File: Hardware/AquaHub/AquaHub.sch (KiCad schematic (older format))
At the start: 73 parts, among them J10 PinHeader6, J13 PinHeader2, J14 PinHeader3, Q2 2SC1815, SW1 SW_Push, SW2 SW_Push, SW3 SW_Push, SW4 SW_Push, SW5 SW_Push, SW6 SW_Push, U1 ESP32-WROOM, U3 1A 3.3V, U4 Low-Side Driver, U5 1A 5V, U6 TCA9534, U7 DS1307+, U8 TPIC2810D, Y1 32.768KHz

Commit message: Commit latest hardware updates and initial firmware
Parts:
- BT1: footprint AquaFootprints:Multicomp-BC-2001 -> Battery:BatteryHolder_Multicomp_BC-2001_1x2032; Mouser (none) -> 534-1058; manf# (none) -> x
- C3: Mouser (none) -> TAJB106K006SNJ; manf# TAJB106K006SNJ -> (none)
- C4: Farnell (none) -> CA06848; Mouser (none) -> TAJD107K006SNJ; manf# TAJD107K006SNJ -> (none)
- C5, C6: Farnell (none) -> CA07886; Mouser (none) -> UWX1H100MCL1GB; manf# UWX1H100MCL1GB -> x
- C7, C8: Mouser (none) -> UWX1H4R7MCL1GB; manf# UWX1H4R7MCL1GB -> x
- C9: Farnell (none) -> CA07658
- LS1: Mouser (none) -> PS1240P02BT; manf# PS1240P02BT -> (none)
- Q2: Farnell (none) -> SC06581
- R10, R11, R12, R13, R14, R15, R16: Farnell (none) -> RE07105; Mouser (none) -> GWCR0603-4K7FT5; manf# GWCR0603-4K7FT5 -> (none)
- R3, R7: Mouser (none) -> GWCR0603-10KFT5; manf# GWCR0603-10KFT5 -> (none)
- R4, R5, R6: manf# GWCR0603-4K7FT5 -> (none)
- R8, R9: Farnell (none) -> RE07090; Mouser (none) -> GWCR0603-4K7FT5; manf# GWCR0603-4K7FT5 -> (none)
- U1: Mouser (none) -> ESP32-WROOM-32D; manf# ESP32-WROOM-32D -> x
- U3: Mouser (none) -> NCP1117DT33G; manf# NCP1117DT33G -> x
- U4: Mouser (none) -> TPL7407LADR; manf# TPL7407LADR -> x
- U5: Mouser (none) -> NCP1117DT50G; manf# NCP1117DT50G -> x
- U6: Mouser (none) -> TCA9534DWR; manf# TCA9534DWR -> x
- U7: manf# (none) -> x
- U8: RS (none) -> 660-7981
- Y1: Mouser (none) -> 815-AB26T-32.768KHZ; manf# (none) -> z

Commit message: Added some more framework
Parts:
- added SW?: Reset, Button_Switch_THT:SW_CK_D6R_SPST_12mm_H14.3mm, symbol AquaHub-rescue:SW_CK_D6R_SPST-Switch
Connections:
- net EN: no longer R3.2, U1.3 (EN)
- net GND: now also SW?.2 (B), SW?.4 (B)
- new net: R3.2, SW?.1 (A), SW?.3 (A), U1.3 (EN)
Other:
- moved on the sheet: C3, C4, R3
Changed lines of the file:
@@
 L AquaHub-rescue:C_Small-Device C3
 U 1 1 5BB06BF9
-P 5525 3250
-F 0 "C3" H 5400 3325 50  0000 L CNN
-F 1 "10uF" H 5325 3175 50  0000 L CNN
-F 2 "Capacitor_SMD:C_0805_2012Metric_Pad1.15x1.40mm_HandSolder" H 5563 3100 50  0001 C CNN
-F 3 "~" H 5525 3250 50  0001 C CNN
-F 4 "Mouser" H 3975 2100 50  0001 C CNN "Vendor"
-F 5 "TAJB106K006SNJ" H 0   0   50  0001 C CNN "Mouser"
-	1    5525 3250
+P 5250 3250
+F 0 "C3" H 5125 3325 50  0000 L CNN
+F 1 "10uF" H 5050 3175 50  0000 L CNN
+F 2 "Capacitor_SMD:C_0805_2012Metric_Pad1.15x1.40mm_HandSolder" H 5288 3100 50  0001 C CNN
+F 3 "~" H 5250 3250 50  0001 C CNN
+F 4 "Mouser" H 3700 2100 50  0001 C CNN "Vendor"
+F 5 "TAJB106K006SNJ" H -275 0   50  0001 C CNN "Mouser"
+	1    5250 3250
 	1    0    0    -1
 $EndComp
@@
 L AquaHub-rescue:CP_Small-Device C4
 U 1 1 5BB06BFF
-P 5725 3250
-F 0 "C4" H 5750 3325 50  0000 L CNN
-F 1 "100uF" H 5750 3175 50  0000 L CNN
-F 2 "Capacitor_Tantalum_SMD:CP_EIA-7343-31_Kemet-D_Pad2.25x2.55mm_HandSolder" H 5763 3100 50  0001 C CNN
-F 3 "~" H 5725 3250 50  0001 C CNN
-F 4 "Mouser" H 3975 2100 50  0001 C CNN "Vendor"
-F 5 "CA06848" H 0   0   50  0001 C CNN "Farnell"
-F 6 "TAJD107K006SNJ" H 0   0   50  0001 C CNN "Mouser"
-	1    5725 3250
-	1    0    0    -1
-$EndComp
-Wire Wire Line
-	5525 3350 5525 3400
-Wire Wire Line
-	5525 3400 5625 3400
-Wire Wire Line
-	5725 3400 5725 3350
-Wire Wire Line
-	5625 3400 5625 3450
-Connection ~ 5625 3400
-Wire Wire Line
-	5625 3400 5725 3400
-Wire Wire Line
-	5525 3150 5525 3100
-Wire Wire Line
-	5525 3100 5625 3100
-Wire Wire Line
-	5725 3100 5725 3150
-Wire Wire Line
-	5625 3100 5625 3050
-Connection ~ 5625 3100
-Wire Wire Line
-	5625 3100 5725 3100
+P 5450 3250
+F 0 "C4" H 5475 3325 50  0000 L CNN
+F 1 "100uF" H 5475 3175 50  0000 L CNN
+F 2 "Capacitor_Tantalum_SMD:CP_EIA-7343-31_Kemet-D_Pad2.25x2.55mm_HandSolder" H 5488 3100 50  0001 C CNN
+F 3 "~" H 5450 3250 50  0001 C CNN
+F 4 "Mouser" H 3700 2100 50  0001 C CNN "Vendor"
+F 5 "CA06848" H -275 0   50  0001 C CNN "Farnell"
+F 6 "TAJD107K006SNJ" H -275 0   50  0001 C CNN "Mouser"
+	1    5450 3250
+	1    0    0    -1
+$EndComp
+Wire Wire Line
+	5250 3350 5250 3400
+Wire Wire Line
+	5250 3400 5350 3400
+Wire Wire Line
+	5450 3400 5450 3350
+Connection ~ 5350 3400
+Wire Wire Line
+	5350 3400 5450 3400
+Wire Wire Line
+	5250 3150 5250 3100
+Wire Wire Line
+	5250 3100 5350 3100
+Wire Wire Line
+	5450 3100 5450 3150
+Wire Wire Line
+	5350 3100 5350 3050
+Connection ~ 5350 3100
+Wire Wire Line
+	5350 3100 5450 3100
 $Comp
 L AquaHub-rescue:GND-power #PWR0106
 U 1 1 5BB06C11
-P 5625 3450
-F 0 "#PWR0106" H 5625 3200 50  0001 C CNN
-F 1 "GND" H 5630 3277 50  0000 C CNN
-F 2 "" H 5625 3450 50  0001 C CNN
-F 3 "" H 5625 3450 50  0001 C CNN
-	1    5625 3450
-	1    0    0    -1
-$EndComp
-Wire Wire Line
-	5625 3050 6150 3050
+P 5350 3500
+F 0 "#PWR0106" H 5350 3250 50  0001 C CNN
+F 1 "GND" H 5355 3327 50  0000 C CNN
+F 2 "" H 5350 3500 50  0001 C CNN
+F 3 "" H 5350 3500 50  0001 C CNN
+	1    5350 3500
+	1    0    0    -1
+$EndComp
 $Comp
 L AquaHub-rescue:Conn_01x02-Connector_Generic J13
@@
 L AquaHub-rescue:R-Device R3
 U 1 1 5BA87CFB
-P 6150 3300
-F 0 "R3" H 6200 3375 50  0000 L CNN
-F 1 "10k" H 6200 3300 50  0000 L CNN
-F 2 "Resistor_SMD:R_0603_1608Metric_Pad1.05x0.95mm_HandSolder" V 6080 3300 50  0001 C CNN
-F 3 "~" H 6150 3300 50  0001 C CNN
-F 4 "Mouser" H 3975 2100 50  0001 C CNN "Vendor"
-F 5 "GWCR0603-10KFT5" H 0   0   50  0001 C CNN "Mouser"
-	1    6150 3300
-	1    0    0    -1
-$EndComp
-Text Label 6150 3500 1    39   ~ 0
-EN
+P 6150 3275
+F 0 "R3" H 6200 3350 50  0000 L CNN
+F 1 "10k" H 6200 3275 50  0000 L CNN
+F 2 "Resistor_SMD:R_0603_1608Metric_Pad1.05x0.95mm_HandSolder" V 6080 3275 50  0001 C CNN
+F 3 "~" H 6150 3275 50  0001 C CNN
+F 4 "Mouser" H 3975 2075 50  0001 C CNN "Vendor"
+F 5 "GWCR0603-10KFT5" H 0   -25 50  0001 C CNN "Mouser"
+	1    6150 3275
+	1    0    0    -1
+$EndComp
 $Comp
 L AquaHub-rescue:R-Device R7
@@
 	7425 4700 7150 4700
 Wire Wire Line
-	6150 3150 6150 3050
+	6150 3125 6150 3050
 Wire Wire Line
 	6150 3050 6350 3050
@@
 	6350 3050 6350 2900
 Wire Wire Line
-	6150 3450 6150 3500
-Connection ~ 6150 3050
+	6150 3425 6150 3450
 Wire Wire Line
 	4875 5300 4900 5300
@@
 NoConn ~ 5350 4000
 NoConn ~ 5350 3900
+$Comp
+L AquaHub-rescue:SW_CK_D6R_SPST-Switch SW?
+U 1 1 5BD9B1CF
+P 5800 3450
+AR Path="/5B8F2634/5BD9B1CF" Ref="SW?"  Part="1"
+AR Path="/5BD9B1CF" Ref="SW?"  Part="1"
+F 0 "SW?" H 5800 3550 50  0000 C CNN
+F 1 "Reset" H 5700 3600 50  0000 L CNN
+F 2 "Button_Switch_THT:SW_CK_D6R_SPST_12mm_H14.3mm" H 5800 3650 50  0001 C CNN
+F 3 "" H 5800 3650 50  0001 C CNN
+F 4 "Mouser" H -1175 -875 50  0001 C CNN "Vendor"
+	1    5800 3450
+	-1   0    0    1
+$EndComp
+Wire Wire Line
+	5350 3050 6150 3050
+Wire Wire Line
+	6150 3450 6000 3450
+Connection ~ 6150 3450
+Wire Wire Line
+	6150 3450 6150 3500
+Wire Wire Line
+	5350 3400 5350 3450
+Wire Wire Line
+	5600 3450 5350 3450
+Connection ~ 5350 3450
+Wire Wire Line
+	5350 3450 5350 3500
+Connection ~ 6150 3050
 $EndSCHEMATC

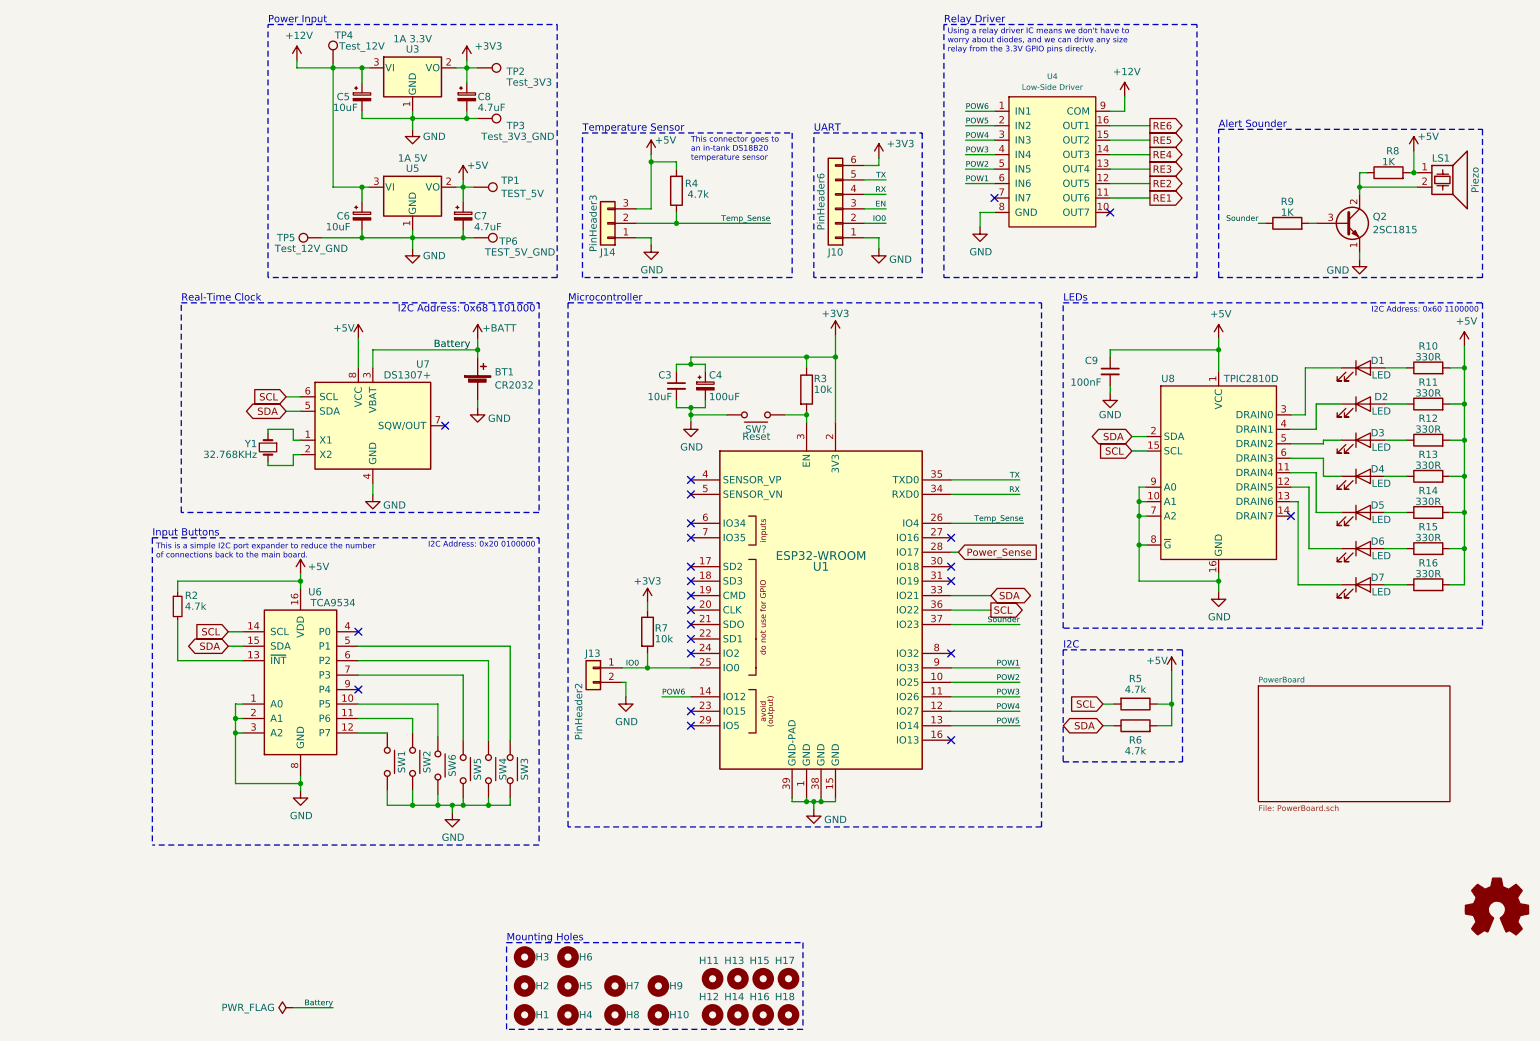
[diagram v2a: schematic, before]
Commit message: Big PCB switch to a single board. Again.
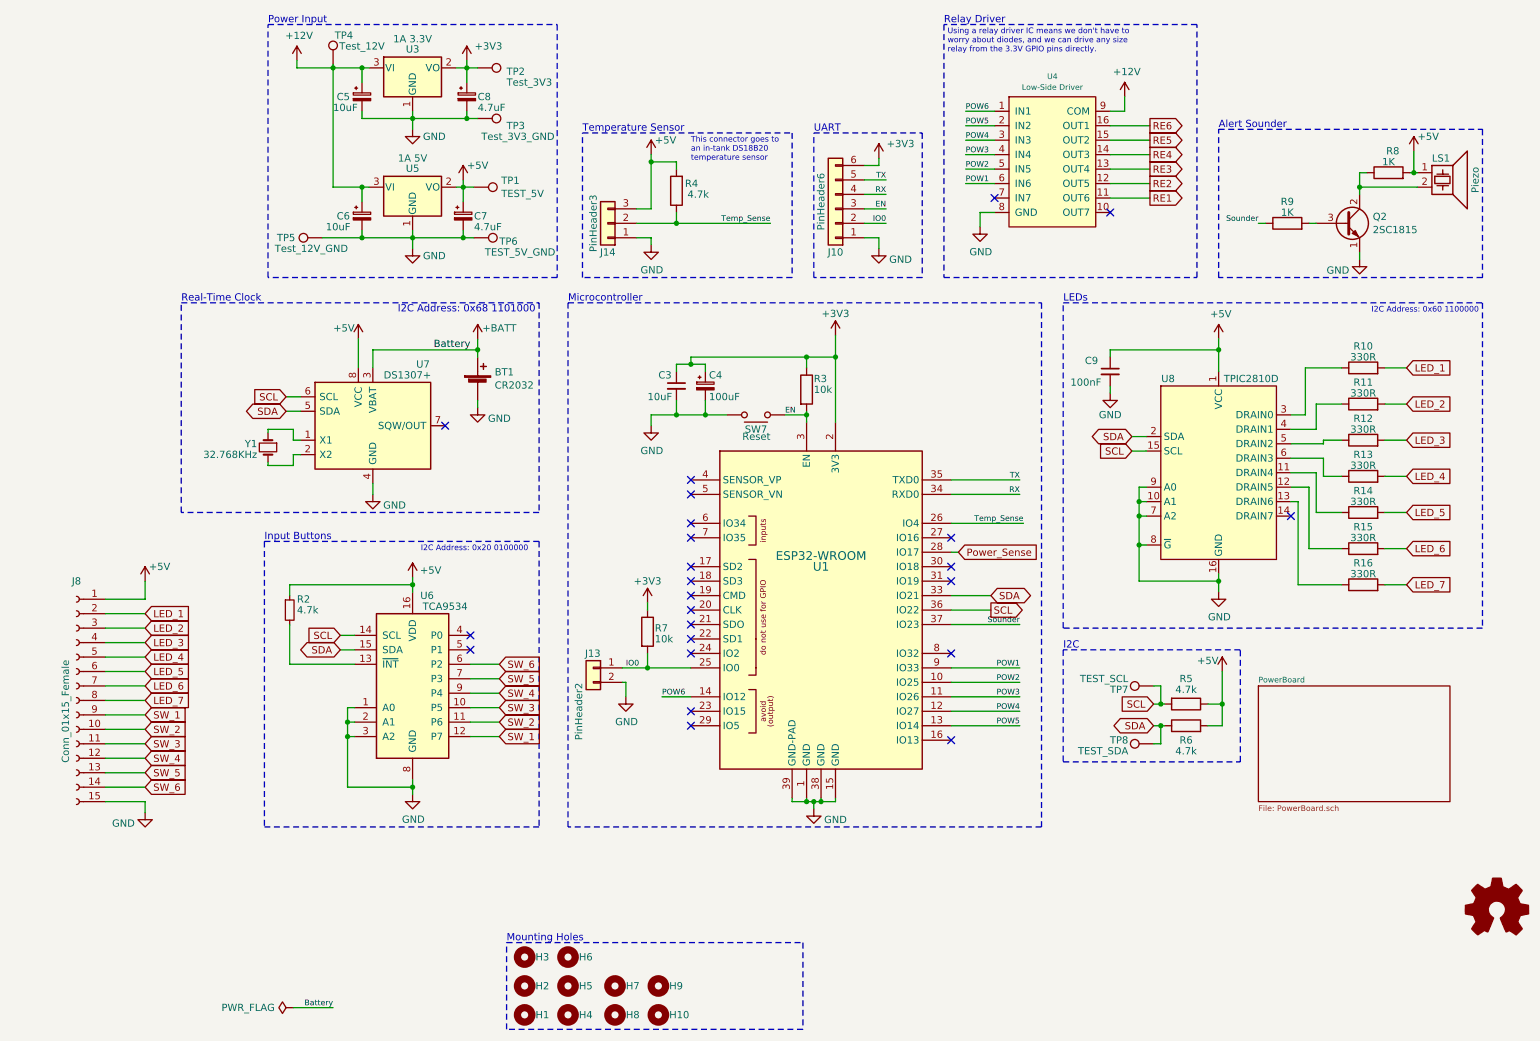
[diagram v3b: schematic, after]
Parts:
- removed D1, D2, D3, D4, D5, D6, D7: LED, LED_THT:LED_D5.0mm, symbol Device:LED
- removed H11, H12, H13, H14, H15, H16, H17, H18: MountingHole, AquaFootprints:Breakaway 1mm, symbol Mechanical:MountingHole
- removed SW1, SW2, SW3, SW4, SW5, SW6: SW_Push, Button_Switch_THT:SW_CK_D6R_SPST_12mm_H14.3mm, symbol AquaHub-rescue:SW_CK_D6R_SPST-Switch
- added J8: Conn_01x15_Female, Connector_Hirose:Hirose_DF52-15S-0.8H_1x15-1MP_P0.80mm_Horizontal, symbol Connector:Conn_01x15_Female
- added TP7: TEST_SCL, TestPoint:TestPoint_Loop_D2.50mm_Drill1.0mm, symbol AquaHub-rescue:TestPoint-Connector
- added TP8: TEST_SDA, TestPoint:TestPoint_Loop_D2.50mm_Drill1.0mm, symbol AquaHub-rescue:TestPoint-Connector
- SW7: renamed from SW?; footprint Button_Switch_THT:SW_CK_D6R_SPST_12mm_H14.3mm -> Button_Switch_SMD:Panasonic_EVQPUJ_EVQPUA
- TP1, TP2, TP3, TP4, TP5, TP6: footprint TestPoint:TestPoint_Keystone_5010-5014_Multipurpose -> TestPoint:TestPoint_Loop_D2.50mm_Drill1.0mm
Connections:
- net +5V: now also J8.1 (Pin_1); no longer R10.2, R11.2, R12.2, R13.2, R14.2, R15.2, R16.2
- net EN: now also R3.2, SW7.1 (A), SW7.3 (A), U1.3 (EN)
- net GND: now also J8.15 (Pin_15)
- net SCL: now also TP7.1
- net SDA: now also TP8.1
- net at R14.1: now also U8.11 (DRAIN4)
- net at R15.1: now also U8.12 (DRAIN5)
- net at R16.1: now also U8.13 (DRAIN6)
- net at R13.1: now also U8.6 (DRAIN3)
- net at R12.1: now also U8.5 (DRAIN2)
- net at R11.1: now also U8.4 (DRAIN1)
- net at R10.1: now also U8.3 (DRAIN0)
- net SW_5: now reaches U6.7 (P3)
- net SW_5: now also J8.13 (Pin_13)
- net SW_3: now reaches U6.10 (P5)
- net SW_3: now also J8.11 (Pin_11)
- net SW_1: now reaches U6.12 (P7)
- net SW_1: now also J8.9 (Pin_9)
- net SW_2: now reaches U6.11 (P6)
- net SW_2: now also J8.10 (Pin_10)
- net SW_6: now reaches U6.6 (P2)
- net SW_6: now also J8.14 (Pin_14)
- net SW_4: now reaches U6.9 (P4)
- net SW_4: now also J8.12 (Pin_12)
- new net LED_1: J8.2 (Pin_2), R10.2
- new net LED_2: J8.3 (Pin_3), R11.2
- new net LED_3: J8.4 (Pin_4), R12.2
- new net LED_4: J8.5 (Pin_5), R13.2
- new net LED_5: J8.6 (Pin_6), R14.2
- new net LED_6: J8.7 (Pin_7), R15.2
- new net LED_7: J8.8 (Pin_8), R16.2
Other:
- note removed: "This is a simple I2C port expander to reduce the number\nof connections back to the main board."
- moved on the sheet: R10, R11, R12, R13, R14, R15, R16, R2, R5, R6, U6

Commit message: Finalising the Rev2 hardware.
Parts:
- removed C4: 100uF, Capacitor_Tantalum_SMD:CP_EIA-7343-31_Kemet-D_Pad2.25x2.55mm_HandSolder, symbol AquaHub-rescue:CP_Small-Device
- removed H10, H9: MountingHole, MountingHole:MountingHole_3.2mm_M3, symbol Mechanical:MountingHole
- removed J13: PinHeader2, Connector_PinHeader_2.54mm:PinHeader_1x02_P2.54mm_Vertical, symbol AquaHub-rescue:Conn_01x02-Connector_Generic
- removed TP3: Test_3V3_GND, TestPoint:TestPoint_Loop_D2.50mm_Drill1.0mm, symbol AquaHub-rescue:TestPoint-Connector
- removed TP5: Test_12V_GND, TestPoint:TestPoint_Loop_D2.50mm_Drill1.0mm, symbol AquaHub-rescue:TestPoint-Connector
- removed Y1: 32.768KHz, Crystal:Crystal_C26-LF_D2.1mm_L6.5mm_Horizontal, symbol AquaHub-rescue:Crystal_Small-Device
- added C10, C11, C4: 0.1uF, Capacitor_SMD:C_0805_2012Metric_Pad1.15x1.40mm_HandSolder, symbol AquaHub-rescue:C_Small-Device
- added R17: 1.5k, Resistor_SMD:R_0603_1608Metric_Pad1.05x0.95mm_HandSolder, symbol Device:R
- added U9: PCT2075, Package_SO:TSOP-6_1.65x3.05mm_P0.95mm, symbol Sensor_Temperature:PCT2075-TSOP6
- added Y1: 32.768KHz, Crystal:Crystal_SMD_SeikoEpson_MC146-4Pin_6.7x1.5mm_HandSoldering, symbol Device:Crystal_GND23
- BT1, C5, C6, C7, C8, U1, U3, U5, U6: manf# x -> (none)
- C9: Mouser (none) -> 710-885012206071
- J10: Mouser (none) -> 710-61300611121
- J14: Mouser (none) -> 710-61300311121
- J8: footprint Connector_Hirose:Hirose_DF52-15S-0.8H_1x15-1MP_P0.80mm_Horizontal -> Connector_PinHeader_2.00mm:PinHeader_2x08_P2.00mm_Vertical; Mouser (none) -> 798-DF51A-16DP-2DSA
- Q2: value 2SC1815 -> 2SC4738; footprint Package_TO_SOT_SMD:SOT-23 -> Package_TO_SOT_SMD:SOT-416; Mouser (none) -> 757-2SC4738-YLF
- R10, R11, R12, R13, R14, R15, R16: Mouser GWCR0603-4K7FT5 -> 603-RC0603FR-07330RL
- R2: symbol Device:R_Small -> Device:R; Mouser (none) -> 603-RC0603FR-074K7L
- R3, R7: Mouser GWCR0603-10KFT5 -> 603-RC0603FR-0710KL
- R4: symbol AquaHub-rescue:R-Device -> Device:R; Mouser (none) -> 603-RC0603FR-074K7L
- R5, R6: Mouser (none) -> 603-RC0603FR-074K7L
- R8, R9: Mouser GWCR0603-4K7FT5 -> 603-RC0603FR-071KL
- SW7: footprint Button_Switch_SMD:Panasonic_EVQPUJ_EVQPUA -> Button_Switch_SMD:SW_SPST_PTS645; Mouser (none) -> 611-PTS645SM43SMTR92
- U4: value Low-Side Driver -> TPL7407LADR; Mouser TPL7407LADR -> 595-TPL7407LADR; manf# x -> (none)
- U7: Mouser (none) -> 700-DS1307ZT&R; manf# x -> (none)
- U8: Mouser (none) -> 595-TPIC2810DR
- renumbered TP6 to TP1, TP1 to TP3
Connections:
- net +3V3: now also C4.1
- net +5V: now also C11.1, R17.1, U9.3 (+Vs)
- net GND: now also C10.2, C11.2, C4.2, U9.1 (A0), U9.2 (GND); no longer SW7.2 (B), SW7.4 (B)
- net SCL: now also U9.4 (SCL)
- net SDA: now also U9.6 (SDA)
- net at U7.1 (X1): now also Y1.1
- net at U7.2 (X2): now also Y1.4
- new net: C10.1, SW7.2 (B), SW7.4 (B)
- new net: R17.2, U9.5 (O.S.)
- no-connect marks 24 -> 26
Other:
- note added: "C1-C3\non the DS"
- note added: "I2C Address: 0x48 1001000"
- note added: "R1 on\nthe DS"
- note added: "Temperature Sense"
- moved on the sheet: C3, R2
